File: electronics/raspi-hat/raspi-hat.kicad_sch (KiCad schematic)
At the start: 22 parts, among them J1 12V from battery, J2 5V to other boards, J3 40HAT, J4 CAN, Q1 DMG2305UX, Q2 DMMT5401, U1 MCP2515-xSO, U2 LD3985M33R_SOT23, U3 MAX33012EASA+, Y1 8MHz

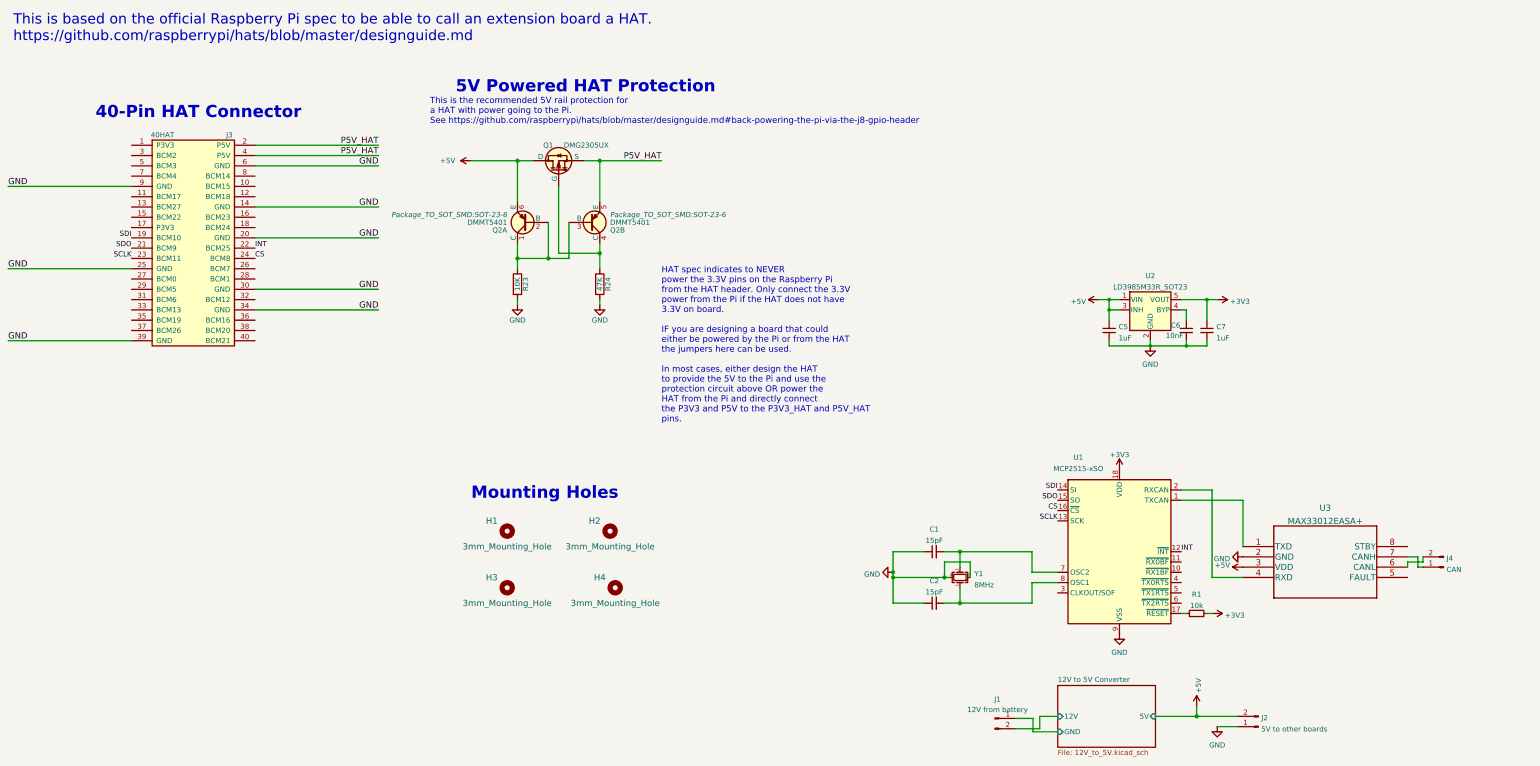
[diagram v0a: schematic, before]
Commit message: Update Raspberry Pi HAT to Rev 2 requirements
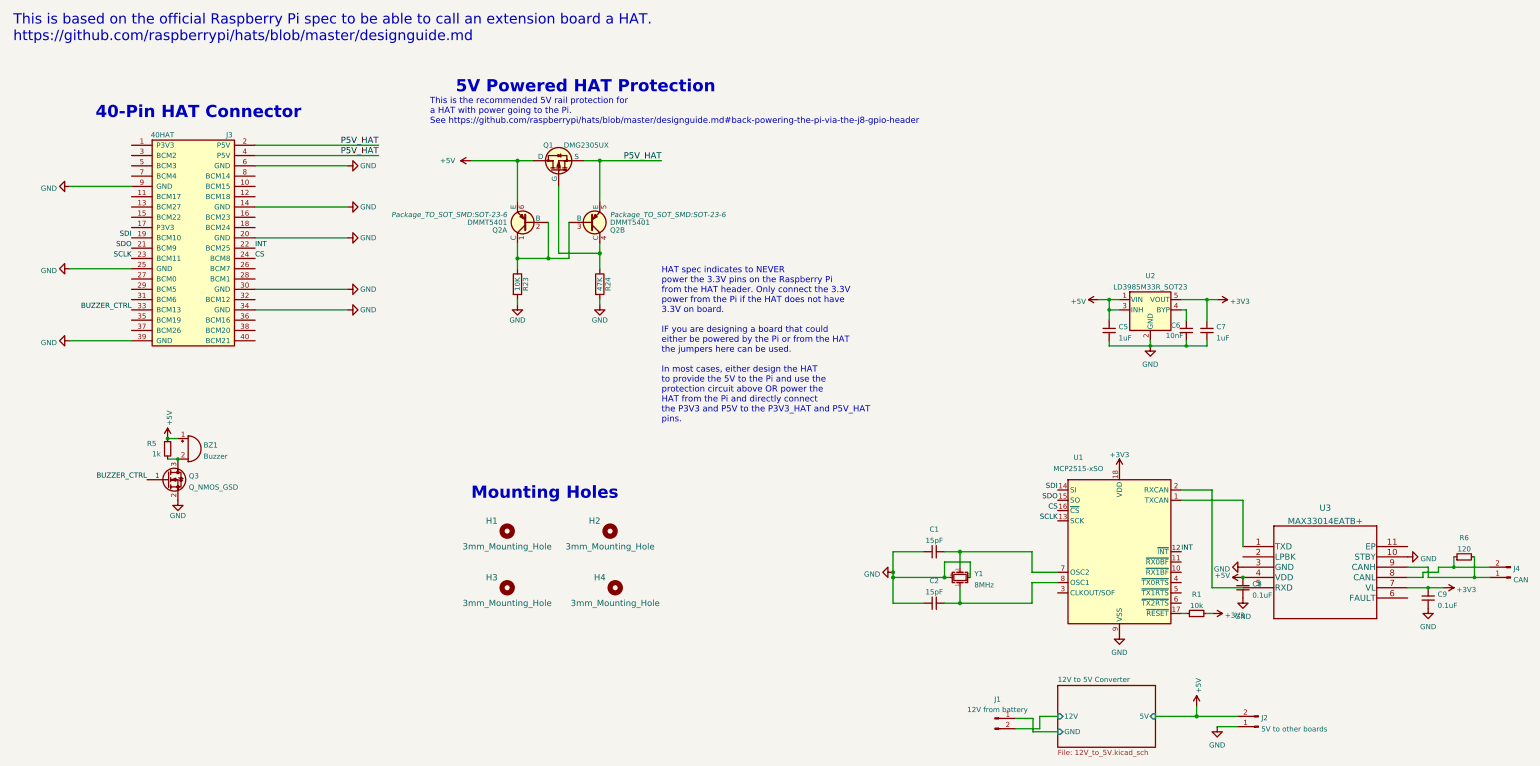
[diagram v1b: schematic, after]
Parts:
- removed U3: MAX33012EASA+, MAX33012EASA+:MAX33012EASA+, symbol MAX33012EASA+:MAX33012EASA+
- added BZ1: Buzzer, PS1420P02CT:PS1420P02CT, symbol Device:Buzzer
- added C8, C9: 0.1uF, Capacitor_SMD:C_0603_1608Metric, symbol Device:C_Small
- added Q3: Q_NMOS_GSD, Package_TO_SOT_SMD:SOT-223, symbol Device:Q_NMOS_GSD
- added R5: 1k, Resistor_SMD:R_0603_1608Metric, symbol Device:R_Small
- added R6: 120, Resistor_SMD:R_0603_1608Metric, symbol Device:R_Small
- added U3: MAX33014EATB+, MAX33014E:MAX33014EATB&plus_, symbol MAX33014EATB+:MAX33014EATB+
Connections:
- net +3V3: now also C9.2, U3.7 (VL)
- net +5V: now also BZ1.1 (-), C8.2, R5.1, U3.4 (VDD)
- net GND: now also C8.1, C9.1, Q3.2 (S), U3.10 (STBY), U3.3 (GND)
- net BUZZER_CTRL: now reaches J3.33 (BCM13)
- net BUZZER_CTRL: now also Q3.1 (G)
- net at U1.1 (TXCAN): now also U3.1 (TXD)
- net at U1.2 (RXCAN): now also U3.5 (RXD)
- net at J4.2 (Pin_2): now also R6.1, U3.8 (CANL)
- net at J4.1 (Pin_1): now also R6.2, U3.9 (CANH)
- new net: BZ1.2 (+), Q3.3 (D), R5.2
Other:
- moved on the sheet: J4

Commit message: Update HAT
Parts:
- Q3: footprint Package_TO_SOT_SMD:SOT-223 -> Package_TO_SOT_SMD:SOT-23
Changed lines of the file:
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@@
       (effects (font (size 1.27 1.27)) (justify left))
     )
-    (property "Footprint" "Package_TO_SOT_SMD:SOT-223" (id 2) (at 64.77 137.16 0)
+    (property "Footprint" "Package_TO_SOT_SMD:SOT-23" (id 2) (at 64.77 137.16 0)
       (effects (font (size 1.27 1.27)) hide)
     )
@@
     )
     (path "/fbf20826-a7f6-4550-bbd0-19e2c0d32370"
-      (reference "Q3") (unit 1) (value "Q_NMOS_GSD") (footprint "Package_TO_SOT_SMD:SOT-223")
+      (reference "Q3") (unit 1) (value "Q_NMOS_GSD") (footprint "Package_TO_SOT_SMD:SOT-23")
     )
     (path "/6d4e5957-6764-40d7-9d3e-e16ba095c79a"

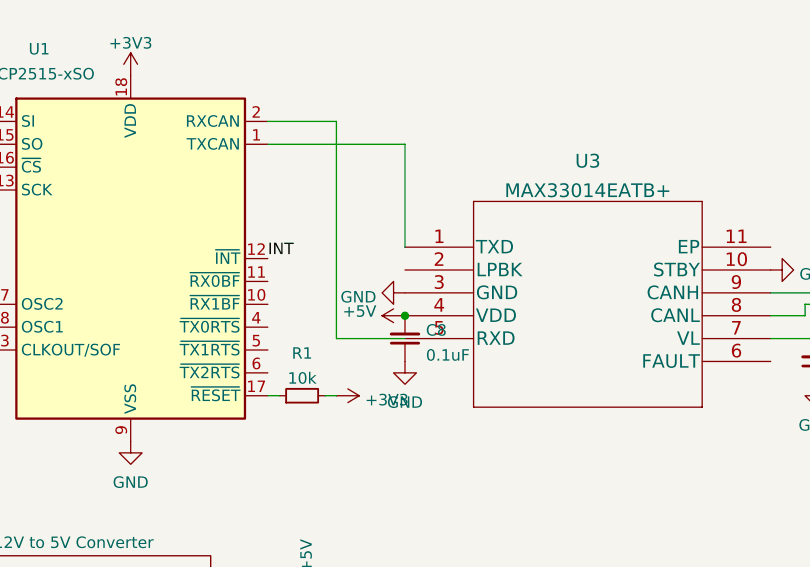
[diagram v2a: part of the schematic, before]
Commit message: Fix DRC errors on Raspi HAT
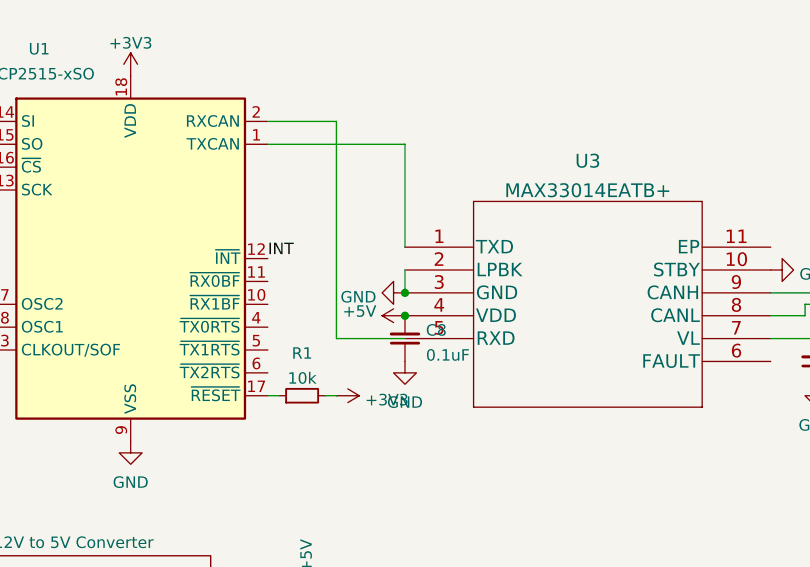
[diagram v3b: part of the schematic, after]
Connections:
- net GND: now also U3.2 (LPBK)
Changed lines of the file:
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@@
   (junction (at 311.15 106.68) (diameter 0) (color 0 0 0 0)
   )
+  (junction (at 325.12 161.29) (diameter 0) (color 0 0 0 0)
+  )
   (junction (at 370.84 166.37) (diameter 0) (color 0 0 0 0)
   )
@@
     (stroke (width 0) (type solid) (color 0 0 0 0))
   )
+  (wire (pts (xy 325.12 158.75) (xy 325.12 161.29))
+    (stroke (width 0) (type default) (color 0 0 0 0))
+  )
   (wire (pts (xy 316.23 95.25) (xy 318.77 95.25))
